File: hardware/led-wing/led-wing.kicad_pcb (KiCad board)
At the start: 2 copper layers, 22.9 x 50 mm, 51 parts, among them J1 Feather, SW1 SW_Push, SW2 SW_Push, SW3 SW_Push, SW4 SW_Push, U1 CD74HC4050

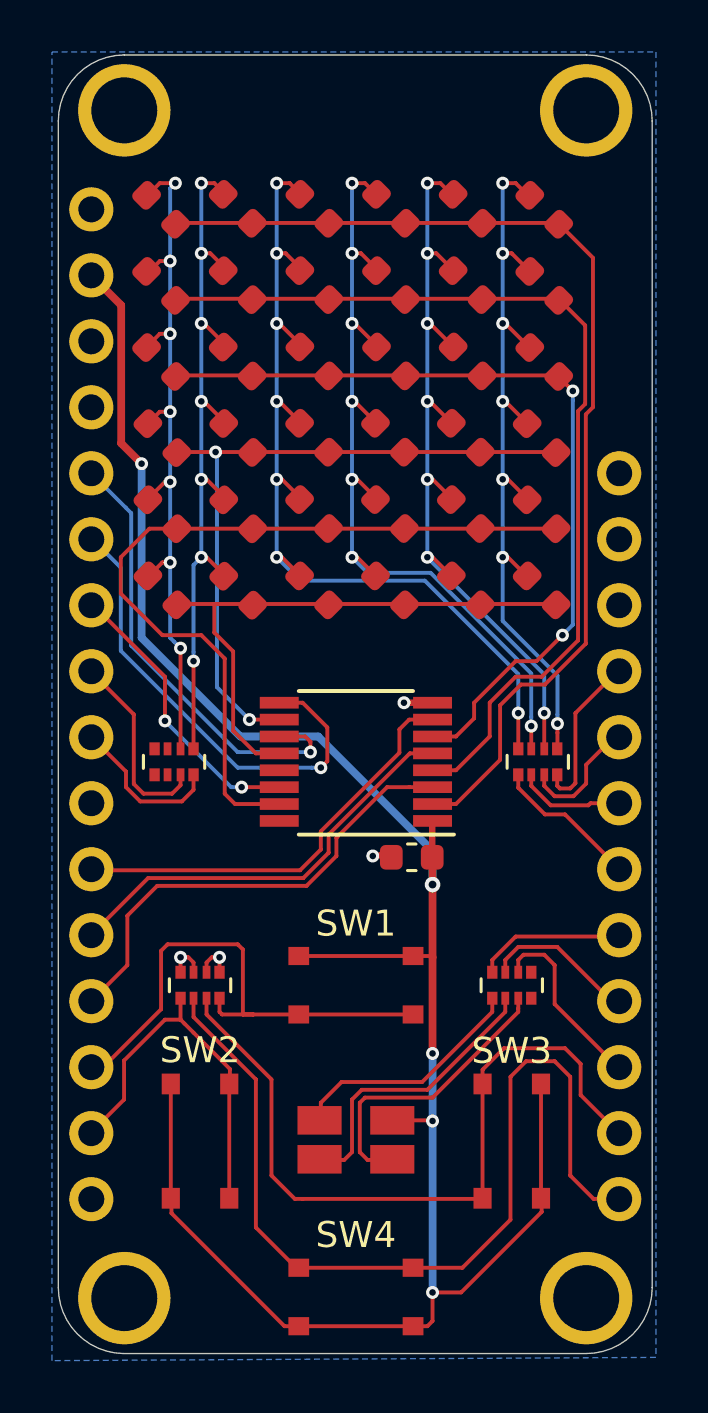
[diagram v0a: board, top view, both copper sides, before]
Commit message: generated gerbers, changed pin labelling to match constraints file
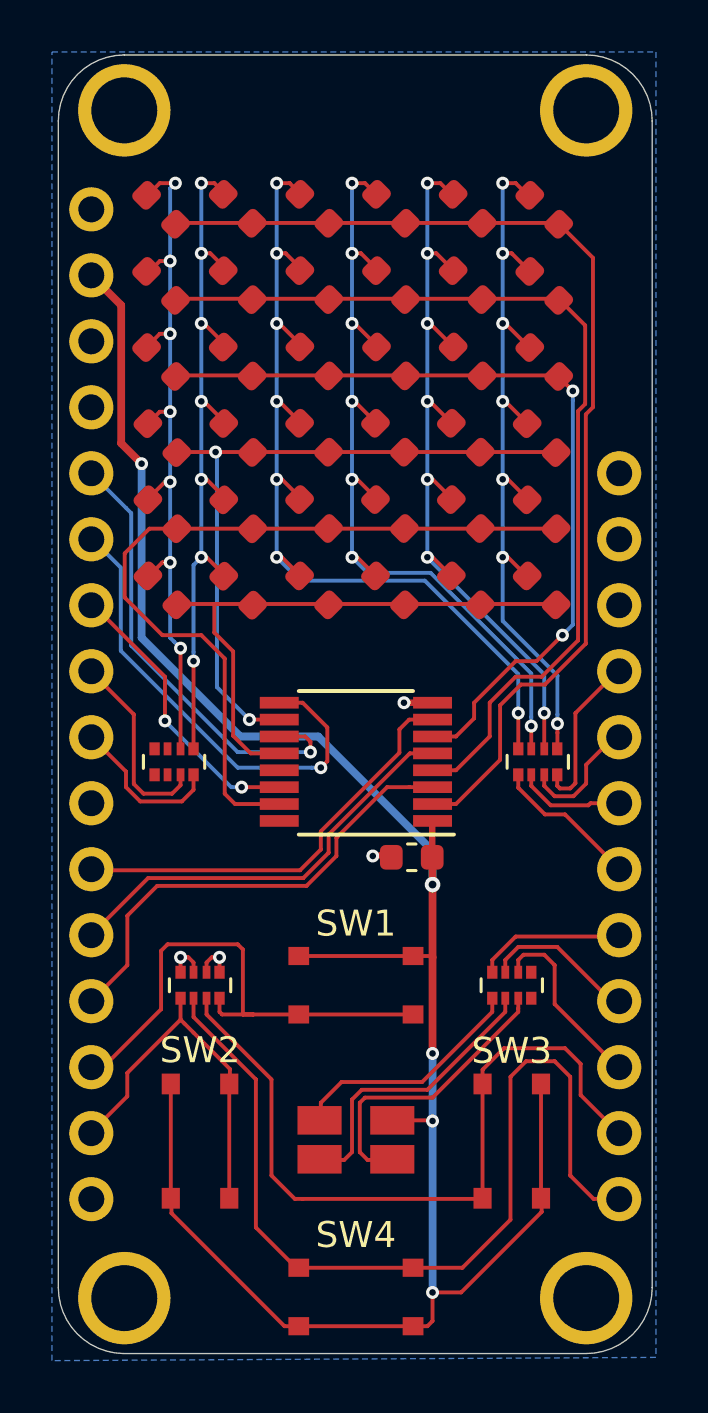
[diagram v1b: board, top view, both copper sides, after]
